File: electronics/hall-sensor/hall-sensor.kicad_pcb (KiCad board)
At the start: 2 copper layers, 30 x 33 mm, 9 parts, among them J1 Conn_01x03, U1 DRV5033AJQLPGM

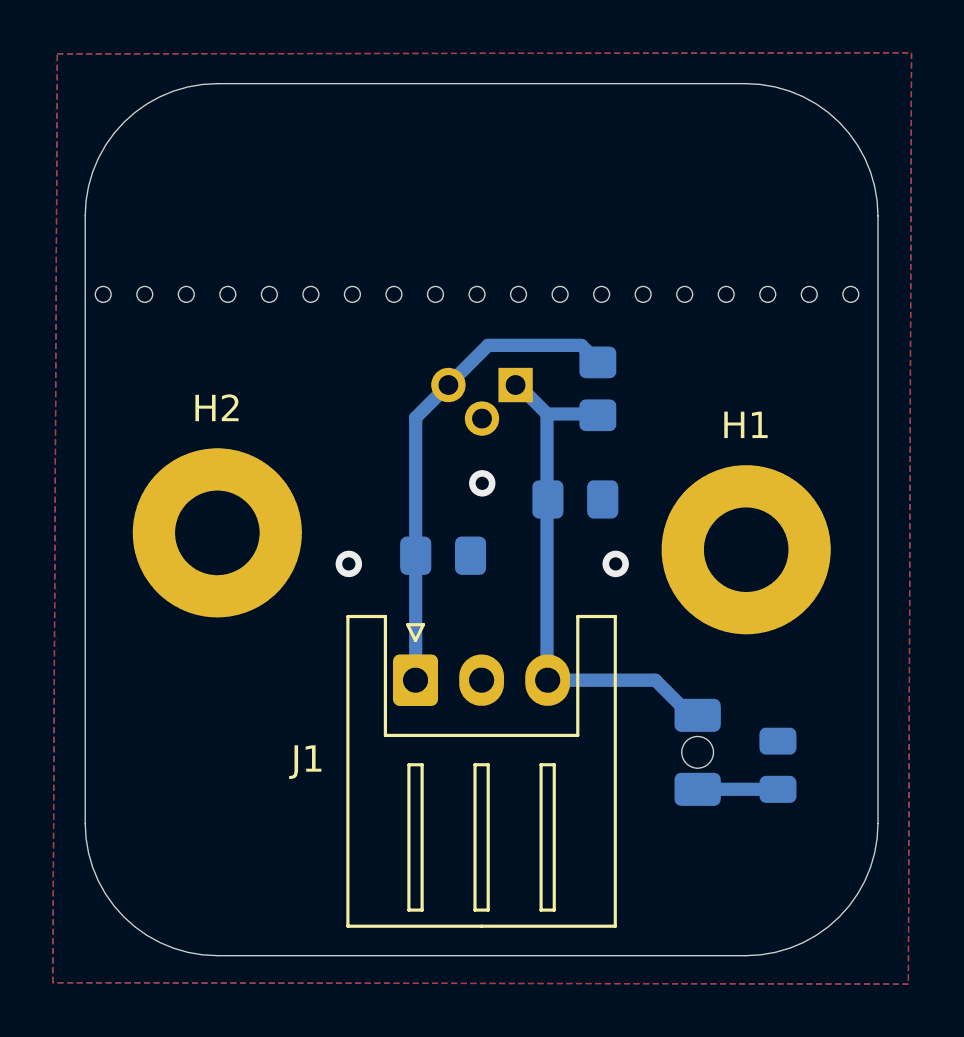
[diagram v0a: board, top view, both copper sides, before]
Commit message: voltage divider added for output pin of hall sensor
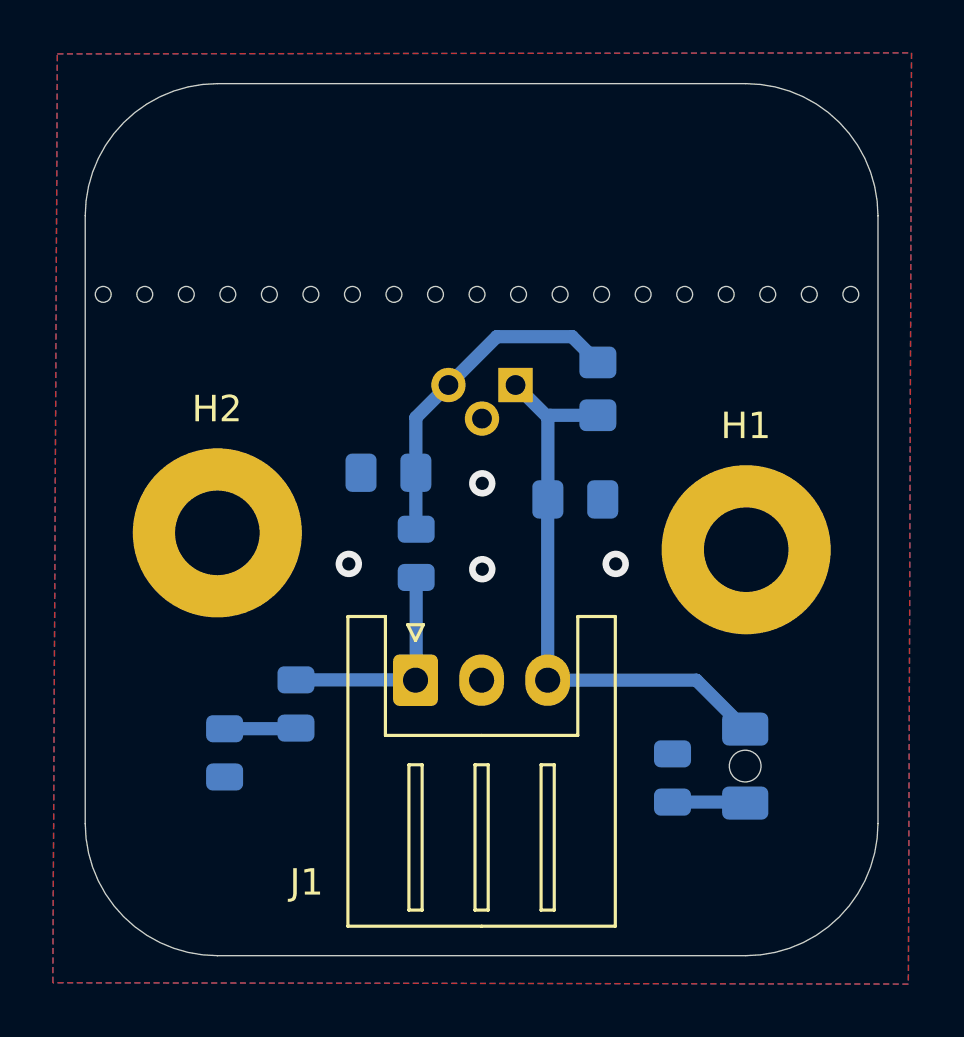
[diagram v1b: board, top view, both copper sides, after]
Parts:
- added R3: 1k, Resistor_SMD:R_0805_2012Metric, B.Cu at (144.3, 94.0)
- added R4: 1k, Resistor_SMD:R_0805_2012Metric, B.Cu at (139.8, 99.7)
- added R5: 1k, Resistor_SMD:R_0805_2012Metric, B.Cu at (137.1, 101.5)
- moved R1 4.02 mm to (154.1, 102.5)
- moved C2 3.76 mm to (143.3, 91.0), turned to 0 degrees
- moved D1 1.87 mm to (156.8, 102.0)
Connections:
- net +3V3 renamed VCC
- C2 pad 2: Net-(J1-Pin_1) -> Net-(U1-OUT)
- R2 pad 1: Net-(J1-Pin_1) -> Net-(U1-OUT)
- U1 pad 3: Net-(J1-Pin_1) -> Net-(U1-OUT)
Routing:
- net Net-(U1-OUT): track 0.00 -> 12.9 mm
- net Net-(J1-Pin_1): track 18.2 -> 8.43 mm
- net Net-(R4-Pad1): track 0.00 -> 2.71 mm
- net VCC: track 19.9 -> 21.8 mm
- net GND: vias 3 -> 4
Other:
- outline, holes or cut-outs redrawn

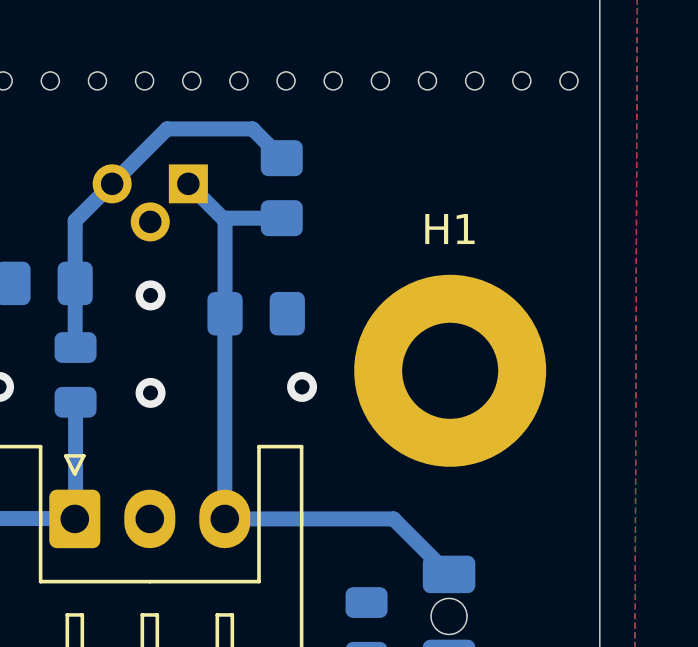
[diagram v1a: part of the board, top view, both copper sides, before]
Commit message: small tweak of mountig hole on hall-sensor board
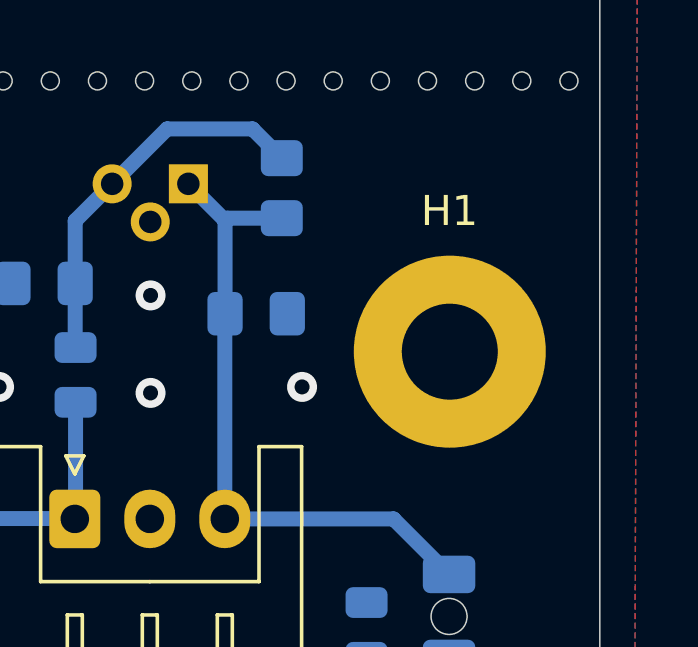
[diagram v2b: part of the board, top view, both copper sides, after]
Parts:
- moved H1 0.64 mm to (156.8, 93.2)
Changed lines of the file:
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@@
 	(footprint "MountingHole:MountingHole_3.2mm_M3_Pad"
 		(layer "F.Cu")
-		(at 156.8375 93.8625)
+		(at 156.825 93.225)
 		(descr "Mounting Hole 3.2mm, M3, generated by kicad-footprint-generator mountinghole.py")
 		(tags "mountinghole M3")
